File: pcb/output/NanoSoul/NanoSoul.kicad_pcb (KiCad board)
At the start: 2 copper layers, 94 x 92 mm, 63 parts, among them J1 JST_PH_B2B-PH-K_1x02_P2.00mm_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, J2 PinHeader_1x02_P2.54mm_Vertic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, J3 PinSocket_1x20_P2.54mm_Vertic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, J4 PinSocket_1x20_P2.54mm_Vertic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, J5 PinHeader_1x06_P2.54mm_Vertic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, J6 PinHeader_1x06_P2.54mm_Vertic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, J7 PinHeader_1x06_P2.54mm_Vertic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, J8 JST_SH_BM04B-SRSS-TB_1x04-1MP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, Q1 SOT-23-6_L2.9-W1.6-P0.95-LS2.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, SW1 SW-SMD_L3.9-W3.0-P4.45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

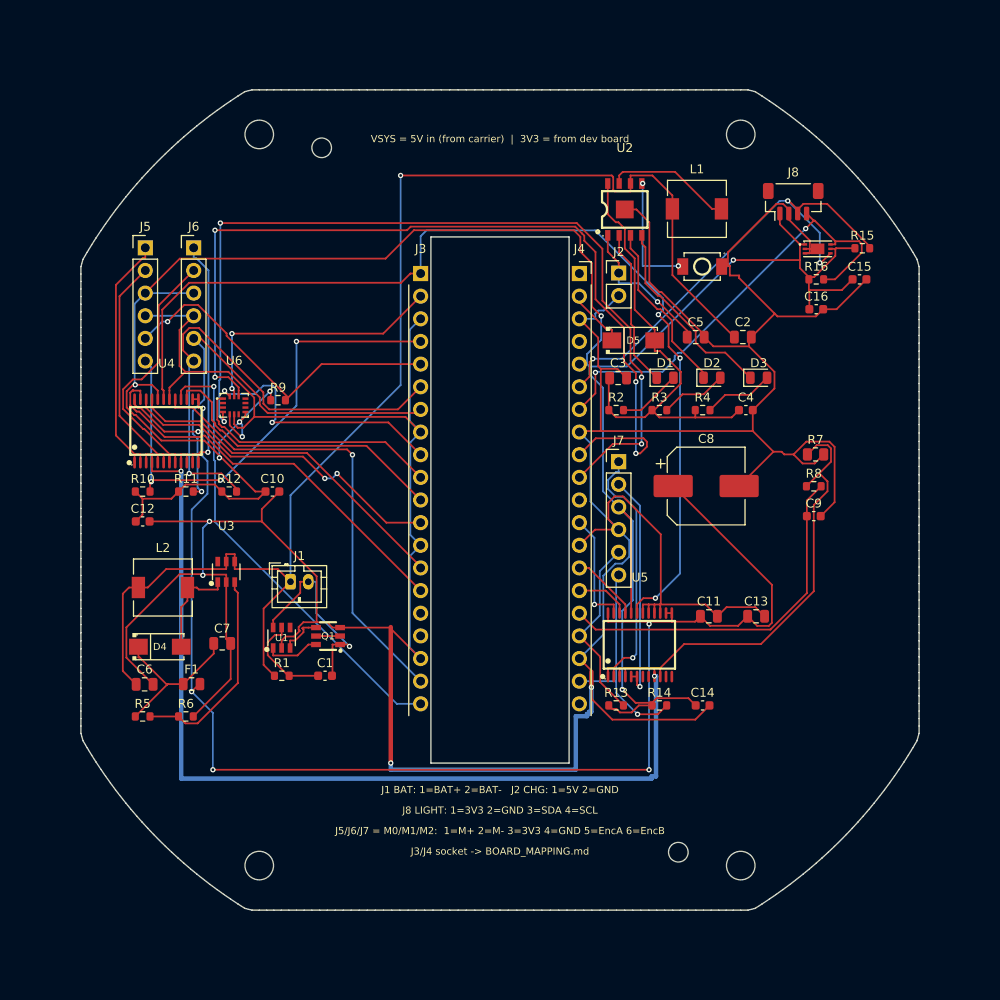
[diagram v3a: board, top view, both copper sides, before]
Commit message: pcb: schematic-parity 真零(零 ignore) + 重导 Gerber
DRC `--schematic-parity --severity-all` = 0 violation / 0 unconnected /
0 schematic-parity,62 项检查全置 error、零 ignore(旧版的 7 项 ignore 全部真修掉,
非关检查)。verify_board 65/65、布线 778 走线+60 过孔未动。

- 修通 circuit-synth 原理图连通性:它把一器件所有网名标签堆在 pin1 → KiCad 推断错网。
  按 .net 逐脚在真实连接点重放 global_label(fix_sch_labels),net_conflict 199→0;
  真 NC 脚在板上配同名 unconnected- 网对齐(assign_nc_nets)。
- 板 Value 回填真实值(顺修「板上 Value=封装名」的 BOM bug)、lib_id 去库前缀(fix_board_meta);
  原理图删 circuit-synth 私有字段/封装过滤器、补缺失 Value(fix_sch_fields);
  J2 attr→through_hole(USB-C 靠屏蔽脚 THT 安装,属实);4×M3 孔标 board_only。
- 唯一保留例外 = J2(USB-C)连接器内部 DRU(实测 0.10mm 铜/0.185mm 孔,JLC 可造;
  KiCad 官方 USB_C_Receptacle_HRO 封装内部孔距也仅 0.15mm → 换封装消不掉、
  改窄焊盘会伤实焊。限 J2 内部两两对象,不放宽对板上走线)。
- 重导 Gerber(9 层 Protel 扩展名 + Excellon 钻孔)+ BOM/CPL。
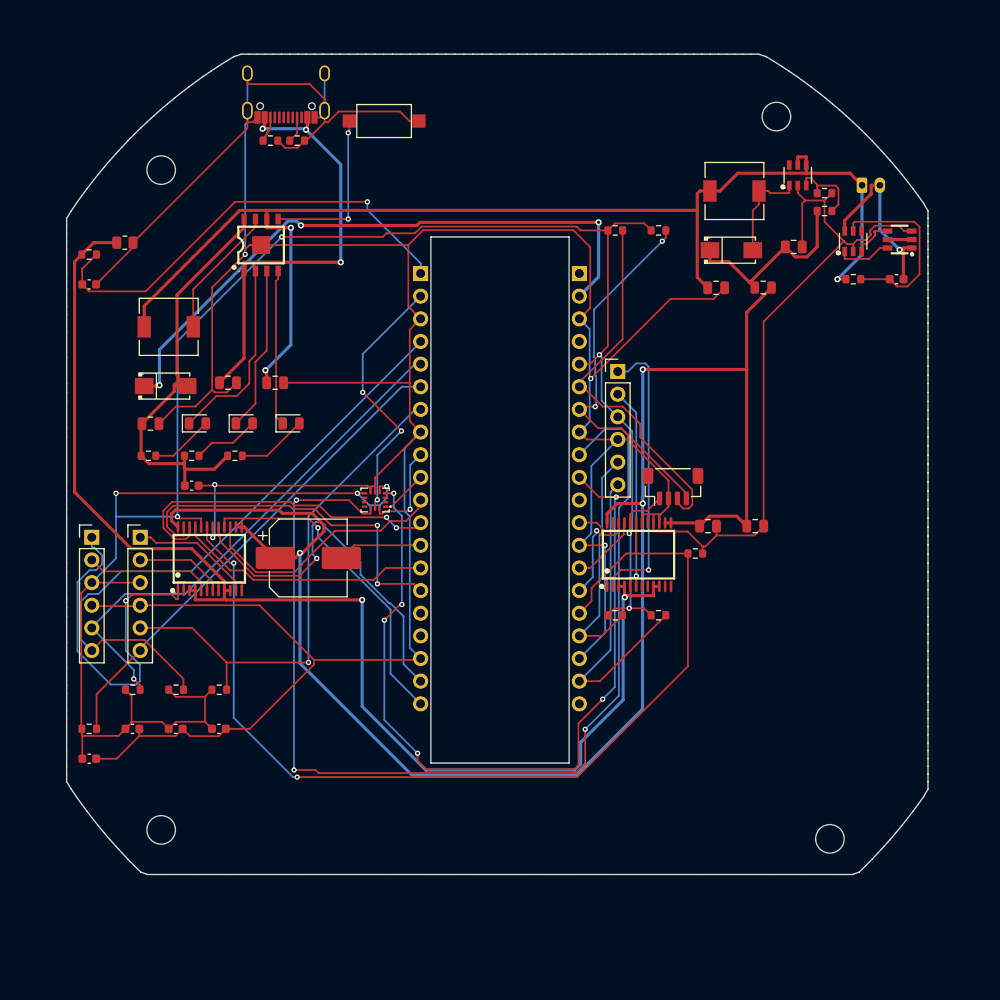
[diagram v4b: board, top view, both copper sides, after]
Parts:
- removed C16: C_0603_1608Metric, C_0603_1608Metric
- removed H5, H6: MountingHole_2.2mm_M2, MountingHole_2.2mm_M2
- removed U7: WSOF-6_L2.6-W1.6-P0.50-TL-EP, WSOF-6_L2.6-W1.6-P0.50-TL-EP
- added R17: 10k, R_0603_1608Metric, F.Cu at (167.8, 112.9)
- added R18: 4.7k, R_0603_1608Metric, F.Cu at (162.9, 69.8)
- added R19: 4.7k, R_0603_1608Metric, F.Cu at (167.8, 69.8)
- C1, C10, C12, C14, C15, C4: value C_0603_1608Metric -> 0.1uF
- C11, C13, C5, C6: value C_0805_2012Metric -> 10uF
- C2, C3, C7: value C_0805_2012Metric -> 22uF
- C8: value CP_Elec_8x10.5 -> 470uF
- C9: value C_0603_1608Metric -> 100nF
- F1: value Fuse_0805_2012Metric -> 1.5A
- J2: value PinHeader_1x02_P2.54mm_Vertical -> USB-C_SMD-TYPE-C-31-M-12_1; footprint PinHeader_1x02_P2.54mm_Vertical -> USB-C_SMD-TYPE-C-31-M-12_1
- L1: value L_6.3x6.3_H3 -> 2.2uH
- L2: value L_6.3x6.3_H3 -> 4.7uH
- R1: value R_0603_1608Metric -> 300
- R10: value R_0603_1608Metric -> 1k
- R11, R12, R13, R14, R15, R16, R8: value R_0603_1608Metric -> 10k
- R2, R3, R4: value R_0603_1608Metric -> 2k
- R5: value 82k -> 5.1k
- R6: value R_0603_1608Metric -> 5.1k
- R7: value R_0805_2012Metric -> 82k; footprint R_0805_2012Metric -> R_0603_1608Metric
- R9: value R_0603_1608Metric -> 0.05; footprint R_0603_1608Metric -> R_0805_2012Metric
- SW1: value SW-SMD_L3.9-W3.0-P4.45 -> SW_SPST_CK_RS282G05A3; footprint SW-SMD_L3.9-W3.0-P4.45 -> SW_SPST_CK_RS282G05A3
- U6: value LGA-14_L3.0-W2.5-P0.50-TL -> LGA-14_L3.0-W2.5-P0.50-BR; footprint LGA-14_L3.0-W2.5-P0.50-TL -> LGA-14_L3.0-W2.5-P0.50-BR
- moved R15 102.1 mm to (103.9, 125.7)
- moved C15 101.7 mm to (103.9, 129.0)
- moved C9 85.3 mm to (103.9, 75.8)
- moved C6 78.0 mm to (174.2, 76.2)
- moved U1 78.0 mm to (189.6, 71.0)
- moved U3 78.0 mm to (183.4, 63.6)
- moved C1 78.0 mm to (194.5, 75.2)
- moved C7 78.0 mm to (182.9, 71.6)
- moved D4 78.0 mm to (175.9, 72.0)
- moved F1 78.0 mm to (179.5, 76.2)
- moved J1 78.0 mm to (190.6, 64.7)
- moved L2 78.0 mm to (176.3, 65.3)
- moved Q1 78.0 mm to (194.8, 70.8)
- moved R1 78.0 mm to (189.6, 75.2)
- moved R5 66.9 mm to (127.2, 59.7)
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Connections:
- J2 pad 1: CHG_IN -> GND
- J3 pad 1: MOTOR_STBY -> MOT_ISENSE
- J4 pad 16: MOT_ISENSE -> MOTOR_STBY
- R10 pad 1: V3V3 -> MOT_RTN
- R10 pad 2: M0_ENC_B -> MOT_ISENSE
- R11 pad 1: V3V3 -> MOTOR_STBY
- R11 pad 2: M1_ENC_A -> GND
- R12 pad 2: M1_ENC_B -> M0_ENC_A
- R13 pad 2: M2_ENC_A -> M0_ENC_B
- R14 pad 2: M2_ENC_B -> M1_ENC_A
- R15 pad 2: I2C1_SDA -> M1_ENC_B
- R16 pad 2: I2C1_SCL -> M2_ENC_A
- R5 pad 1: VMOT -> USB_CC1
- R5 pad 2: MT_FB -> GND
- R6 pad 1: MT_FB -> USB_CC2
- R7 pad 1: MOT_RTN -> VMOT
- R7 pad 2: GND -> MT_FB
- R8 pad 1: MOT_RTN -> MT_FB
- R8 pad 2: MOT_ISENSE -> GND
- R9 pad 1: V3V3 -> MOT_RTN
- R9 pad 2: M0_ENC_A -> GND
- U1 pad 4: (no net) -> unconnected-(U1-TD-Pad4)
- U3 pad 6: (no net) -> unconnected-(U3-NC-Pad6)
- U5 pad 11: (no net) -> unconnected-(U5-BO1-Pad11)
- U5 pad 12: (no net) -> unconnected-(U5-BO1-Pad12)
- U5 pad 7: (no net) -> unconnected-(U5-BO2-Pad7)
- U5 pad 8: (no net) -> unconnected-(U5-BO2-Pad8)
- U6 pad 10: (no net) -> unconnected-(U6-CS-AUX-Pad10)
- U6 pad 11: (no net) -> unconnected-(U6-SDO-SUX-Pad11)
- U6 pad 2: (no net) -> unconnected-(U6-SDX-Pad2)
- U6 pad 3: (no net) -> unconnected-(U6-SCX-Pad3)
- U6 pad 7: (no net) -> GND
- U6 pad 9: (no net) -> unconnected-(U6-INT2-Pad9)
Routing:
- net VSYS: track 6.81 -> 70.5 mm, vias 0 -> 3
- net CHG_IN: track 16.5 -> 49.7 mm, vias 1 -> 3
- net GND: track 483.3 -> 508.0 mm, vias 4 -> 5
- net IMU_MISO: track 28.7 -> 5.30 mm
- net VMOT_F: track 163.5 -> 185.4 mm, vias 6 -> 3
- net V3V3: track 269.0 -> 248.6 mm
- net M0_ENC_A: track 38.9 -> 58.4 mm
- net MOT_RTN: track 161.8 -> 142.8 mm
- net IMU_CS: track 100.0 -> 118.9 mm, vias 4 -> 3
- net IMU_MOSI: track 29.3 -> 10.8 mm, vias 2 -> 1
- net M1_OUT_B: track 30.2 -> 12.7 mm
- net M1_IN2: track 51.6 -> 36.4 mm
- net M0_OUT_A: track 28.1 -> 43.3 mm, vias 0 -> 1
- net MT_FB: track 23.5 -> 8.67 mm
- net M0_ENC_B: track 55.9 -> 70.0 mm, vias 3 -> 0
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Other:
- board size 94 x 92 mm -> 96.6 x 92 mm
- board text removed: "J1 BAT: 1=BAT+ 2=BAT- J2 CHG: 1=5V 2=GND"
- board text removed: "J3/J4 socket -> BOARD_MAPPING.md"
- board text removed: "J5/J6/J7 = M0/M1/M2: 1=M+ 2=M- 3=3V3 4=GND 5=EncA 6=EncB"
- board text removed: "J8 LIGHT: 1=3V3 2=GND 3=SDA 4=SCL"
- board text removed: "VSYS = 5V in (from carrier) | 3V3 = from dev board"

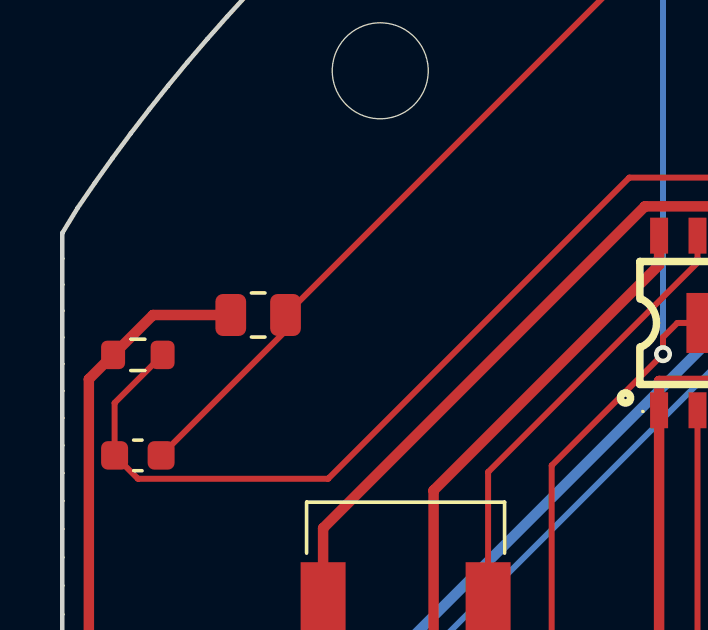
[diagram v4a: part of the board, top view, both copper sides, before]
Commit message: pcb: 修嘉立创 SMT 单两处"邮寄/停产"料 — U6→QMI8658A、R9 shunt→1206
SMT 下单核对单 待邮寄(2): U6 IMU 停产、R9 shunt 无现货。改为全现货可自动贴装：

- U6 IMU: QMI8658C(C2842151,JLC SMT 停产/邮寄) → 同族 QMI8658A(C3021082,
  现货 39k)。同 LGA-14、4 线 SPI 脚位完全一致(A 版 datasheet 13-52-25
  Table3+Fig4 逐脚核过:1=SDO/4=INT1/5=VDDIO/6,7=GND/8=VDD/12=CS/13=SCL/
  14=SDA,2/3/9/10/11 SPI 下可悬空)、驱动同(SensorLib/Waveshare)→ 板/固件不动,仅换料号。
- R9 50mΩ 电流采样 shunt: 0805 50mΩ 在 JLC 无现货(UNI-ROYAL C127697 仅 4 颗、
  Yageo 0805 R05L 不在库) → 改 1206 Yageo RL1206FR-070R05L(C375525,现货 15k/250mW/
  AEC-Q200)。板上【原地换封装】(焊盘 1.125×1.75、丝印/courtyard/fab 几何全取官方
  R_1206_3216Metric)，阻值 50mΩ 不变、位置/网络不变;开放区无邻件、走线仍连通。
- DRC --schematic-parity --severity-all = 0/0/0、parity 0、verify_board 65/65 不变。
- 重导 Gerber(9 层 Protel)+ BOM/CPL;BOM 30 行全带 LCSC、全现货(无留空/邮寄/停产)。
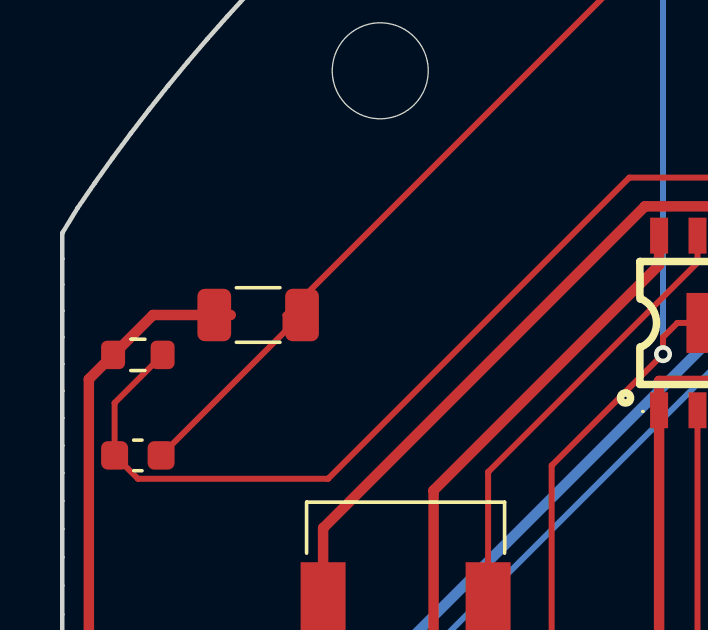
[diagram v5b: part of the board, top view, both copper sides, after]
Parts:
- R9: footprint R_0805_2012Metric -> R_1206_3216Metric
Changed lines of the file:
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@@
 		)
 	)
-	(footprint "R_0805_2012Metric"
+	(footprint "R_1206_3216Metric"
 		(layer "F.Cu")
 		(at 107.93 71.14)
@@
 		(duplicate_pad_numbers_are_jumpers no)
 		(fp_line
-			(start -0.227064 -0.735)
-			(end 0.227064 -0.735)
+			(start -0.727064 -0.91)
+			(end 0.727064 -0.91)
 			(stroke
 				(width 0.12)
-				(type solid)
+				(type default)
 			)
 			(layer "F.SilkS")
 		)
 		(fp_line
-			(start -0.227064 0.735)
-			(end 0.227064 0.735)
+			(start -0.727064 0.91)
+			(end 0.727064 0.91)
 			(stroke
 				(width 0.12)
-				(type solid)
+				(type default)
 			)
 			(layer "F.SilkS")
 		)
 		(fp_rect
-			(start -1.68 -0.95)
-			(end 1.68 0.95)
+			(start -2.28 -1.13)
+			(end 2.28 1.13)
 			(stroke
 				(width 0.05)
-				(type solid)
+				(type default)
 			)
 			(fill no)
@@
 		)
 		(fp_rect
-			(start -1 -0.625)
-			(end 1 0.625)
+			(start -1.6 -0.8)
+			(end 1.6 0.8)
 			(stroke
 				(width 0.1)
-				(type solid)
+				(type default)
 			)
 			(fill no)
@@
 		)
 		(pad "1" smd roundrect
-			(at -0.9125 0)
-			(size 1.025 1.4)
+			(at -1.4625 0)
+			(size 1.125 1.75)
 			(layers "F.Cu" "F.Mask" "F.Paste")
-			(roundrect_rratio 0.243902)
+			(roundrect_rratio 0.222222)
 			(net "MOT_RTN")
 		)
 		(pad "2" smd roundrect
-			(at 0.9125 0)
-			(size 1.025 1.4)
+			(at 1.4625 0)
+			(size 1.125 1.75)
 			(layers "F.Cu" "F.Mask" "F.Paste")
-			(roundrect_rratio 0.243902)
+			(roundrect_rratio 0.222222)
 			(net "GND")
 		)
